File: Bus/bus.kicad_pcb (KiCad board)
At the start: 4 copper layers, 62.2 x 274.1 mm, 54 parts, among them J1 Conn_01x05_Pin, J10 Conn_01x10_Pin, J11 Conn_01x05_Pin, J12 Conn_01x07_Pin, J13 Conn_01x08_Pin, J14 Conn_01x08_Pin, J15 Conn_01x06_Pin, J16 Conn_01x03_Pin, J17 Conn_01x10_Pin, J18 Conn_01x03_Pin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

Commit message: Minor silkscreen updates
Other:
- board text added: "Memory Address Register"
- board text removed: "Memory Access Register"
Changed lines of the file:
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@@
 		)
 		(property "Footprint" "_DownloadFootprints:CF_series_Resistors_THT"
-			(at 0 0 360)
+			(at 0 0 0)
 			(layer "F.Fab")
 			(hide yes)
@@
 		)
 		(property "Datasheet" ""
-			(at 0 0 360)
+			(at 0 0 0)
 			(layer "F.Fab")
 			(hide yes)
@@
 		)
 		(property "Description" "Resistor"
-			(at 0 0 360)
+			(at 0 0 0)
 			(layer "F.Fab")
 			(hide yes)
@@
 		)
 		(property "Footprint" "_DownloadFootprints:CF_series_Resistors_THT"
-			(at 0 0 360)
+			(at 0 0 0)
 			(layer "F.Fab")
 			(hide yes)
@@
 		)
 		(property "Datasheet" ""
-			(at 0 0 360)
+			(at 0 0 0)
 			(layer "F.Fab")
 			(hide yes)
@@
 		)
 		(property "Description" "Resistor"
-			(at 0 0 360)
+			(at 0 0 0)
 			(layer "F.Fab")
 			(hide yes)
@@
 		)
 		(property "Footprint" "_DownloadFootprints:CF_series_Resistors_THT"
-			(at 0 0 360)
+			(at 0 0 0)
 			(layer "F.Fab")
 			(hide yes)
@@
 		)
 		(property "Datasheet" ""
-			(at 0 0 360)
+			(at 0 0 0)
 			(layer "F.Fab")
 			(hide yes)
@@
 		)
 		(property "Description" "Resistor"
-			(at 0 0 360)
+			(at 0 0 0)
 			(layer "F.Fab")
 			(hide yes)
@@
 		)
 		(property "Footprint" "_DownloadFootprints:CF_series_Resistors_THT"
-			(at 0 0 360)
+			(at 0 0 0)
 			(layer "F.Fab")
 			(hide yes)
@@
 		)
 		(property "Datasheet" ""
-			(at 0 0 360)
+			(at 0 0 0)
 			(layer "F.Fab")
 			(hide yes)
@@
 		)
 		(property "Description" "Resistor"
-			(at 0 0 360)
+			(at 0 0 0)
 			(layer "F.Fab")
 			(hide yes)
@@
 		)
 		(property "Footprint" "_DownloadFootprints:CF_series_Resistors_THT"
-			(at 0 0 360)
+			(at 0 0 0)
 			(layer "F.Fab")
 			(hide yes)
@@
 		)
 		(property "Datasheet" ""
-			(at 0 0 360)
+			(at 0 0 0)
 			(layer "F.Fab")
 			(hide yes)
@@
 		)
 		(property "Description" "Resistor"
-			(at 0 0 360)
+			(at 0 0 0)
 			(layer "F.Fab")
 			(hide yes)
@@
 		)
 		(property "Footprint" "_DownloadFootprints:CF_series_Resistors_THT"
-			(at 0 0 360)
+			(at 0 0 0)
 			(layer "F.Fab")
 			(hide yes)
@@
 		)
 		(property "Datasheet" ""
-			(at 0 0 360)
+			(at 0 0 0)
 			(layer "F.Fab")
 			(hide yes)
@@
 		)
 		(property "Description" "Resistor"
-			(at 0 0 360)
+			(at 0 0 0)
 			(layer "F.Fab")
 			(hide yes)
@@
 		)
 		(property "Footprint" "_DownloadFootprints:CF_series_Resistors_THT"
-			(at 0 0 360)
+			(at 0 0 0)
 			(layer "F.Fab")
 			(hide yes)
@@
 		)
 		(property "Datasheet" ""
-			(at 0 0 360)
+			(at 0 0 0)
 			(layer "F.Fab")
 			(hide yes)
@@
 		)
 		(property "Description" "Resistor"
-			(at 0 0 360)
+			(at 0 0 0)
 			(layer "F.Fab")
 			(hide yes)
@@
 		)
 		(property "Footprint" "_DownloadFootprints:CF_series_Resistors_THT"
-			(at 0 0 360)
+			(at 0 0 0)
 			(layer "F.Fab")
 			(hide yes)
@@
 		)
 		(property "Datasheet" ""
-			(at 0 0 360)
+			(at 0 0 0)
 			(layer "F.Fab")
 			(hide yes)
@@
 		)
 		(property "Description" "Resistor"
-			(at 0 0 360)
+			(at 0 0 0)
 			(layer "F.Fab")
 			(hide yes)
@@
 		)
 	)
-	(gr_text "Memory\nAccess\nRegister"
+	(gr_text "Memory\nAddress\nRegister"
 		(at 127.508 110.744 0)
 		(layer "F.SilkS")

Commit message: Connected unused control pins (B out/Output 2's Complement) to disabled values instead of floating
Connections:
- J22 pad 1: /Output/2C -> GND
- J5 pad 1: /BRegister/~Write -> +5V
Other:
- board text removed: "2C"

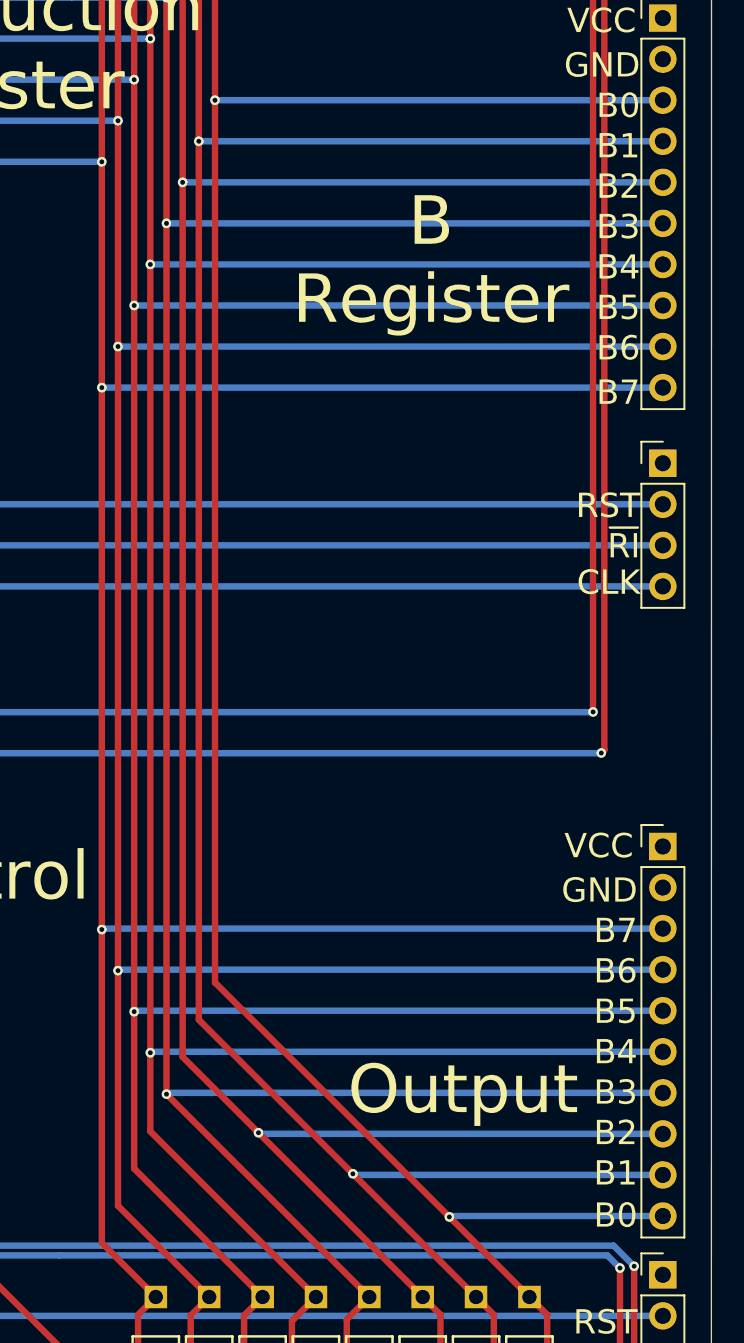
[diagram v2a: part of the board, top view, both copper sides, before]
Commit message: Ouput bus was labeled incorectly. Labels fixed on output. Labels and connections fixed on bus
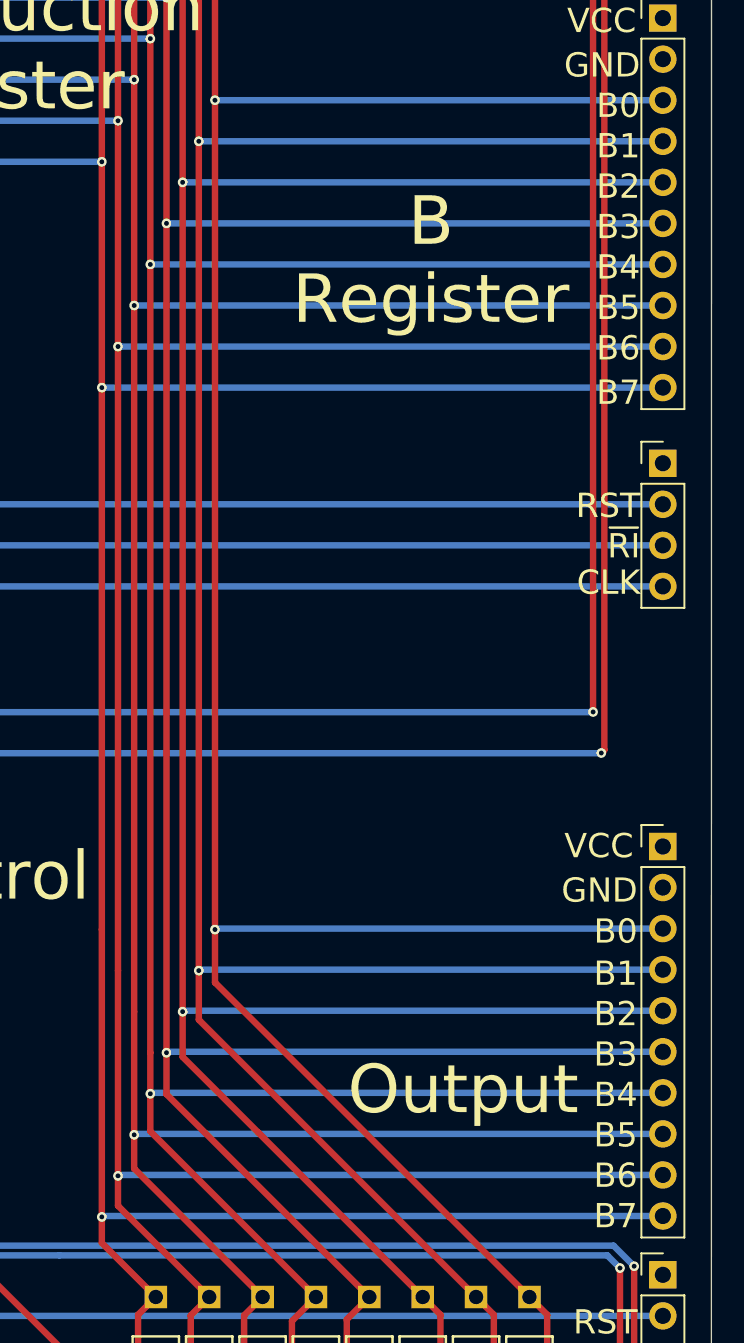
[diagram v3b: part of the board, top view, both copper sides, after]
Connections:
- J21 pad 10: /B0 -> /B7
- J21 pad 3: /B7 -> /B0
- J21 pad 4: /B6 -> /B1
- J21 pad 5: /B5 -> /B2
- J21 pad 6: /B4 -> /B3
- J21 pad 7: /B3 -> /B4
- J21 pad 8: /B2 -> /B5
- J21 pad 9: /B1 -> /B6
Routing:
- net /B0: track 484.5 -> 499.0 mm
- net /B1: track 484.5 -> 494.0 mm
- net /B2: track 484.4 -> 489.1 mm
